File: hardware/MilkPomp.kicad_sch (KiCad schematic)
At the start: 0 parts

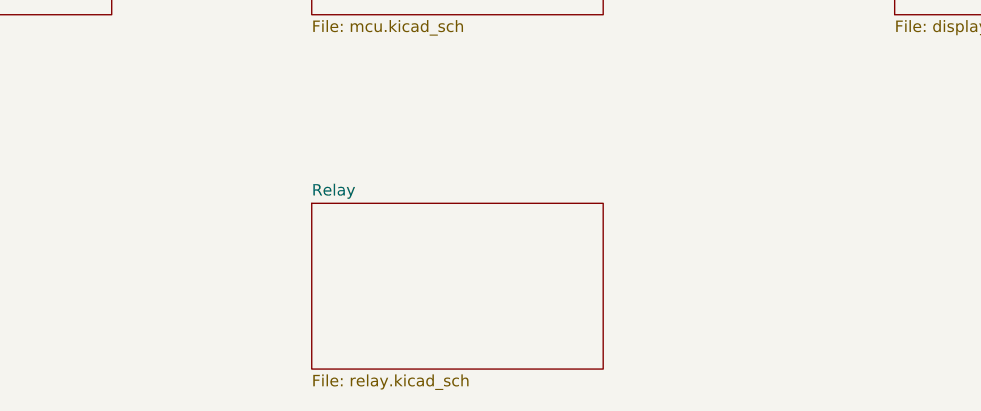
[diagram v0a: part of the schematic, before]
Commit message: Relay module completed
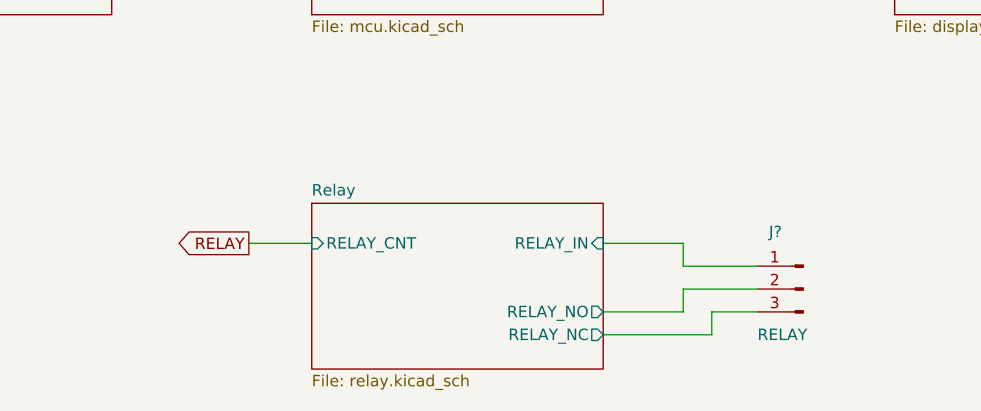
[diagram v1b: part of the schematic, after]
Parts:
- added J?: RELAY, symbol Connector:Conn_01x03_Male
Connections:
- new net Relay/RELAY_IN: J?.1 (Pin_1)
- new net Relay/RELAY_NC: J?.3 (Pin_3)
- new net Relay/RELAY_NO: J?.2 (Pin_2)
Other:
- sheet Relay ports: added RELAY_CNT, RELAY_IN, RELAY_NC, RELAY_NO; removed none

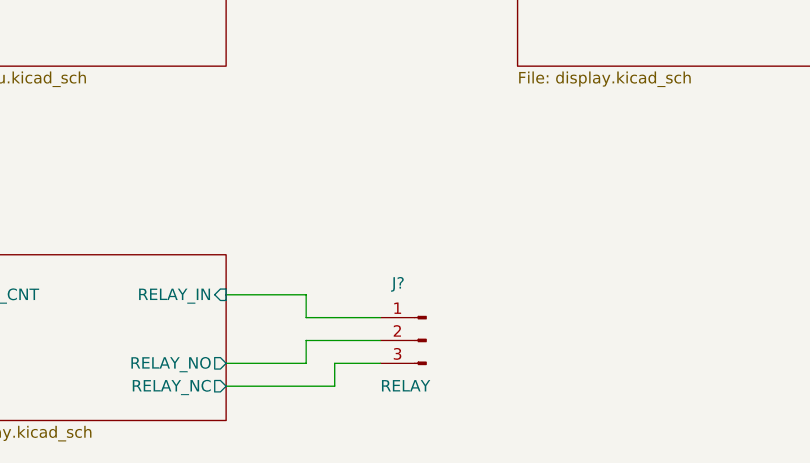
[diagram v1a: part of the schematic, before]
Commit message: Display circuit added
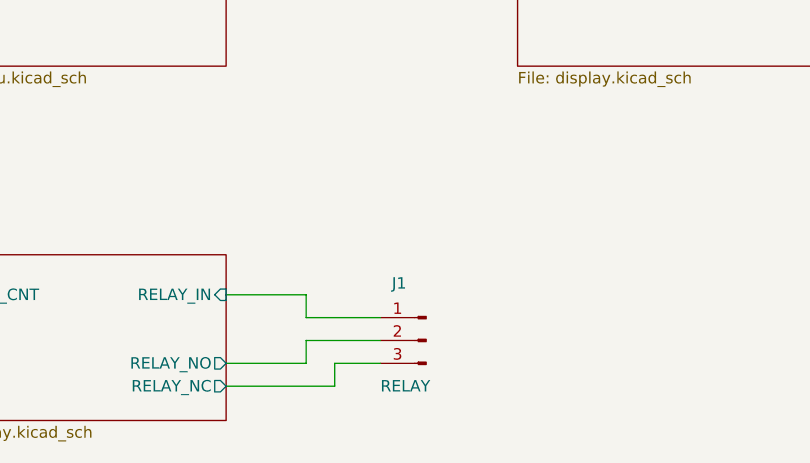
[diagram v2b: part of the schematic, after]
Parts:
- gave numbers to parts that had none: 1

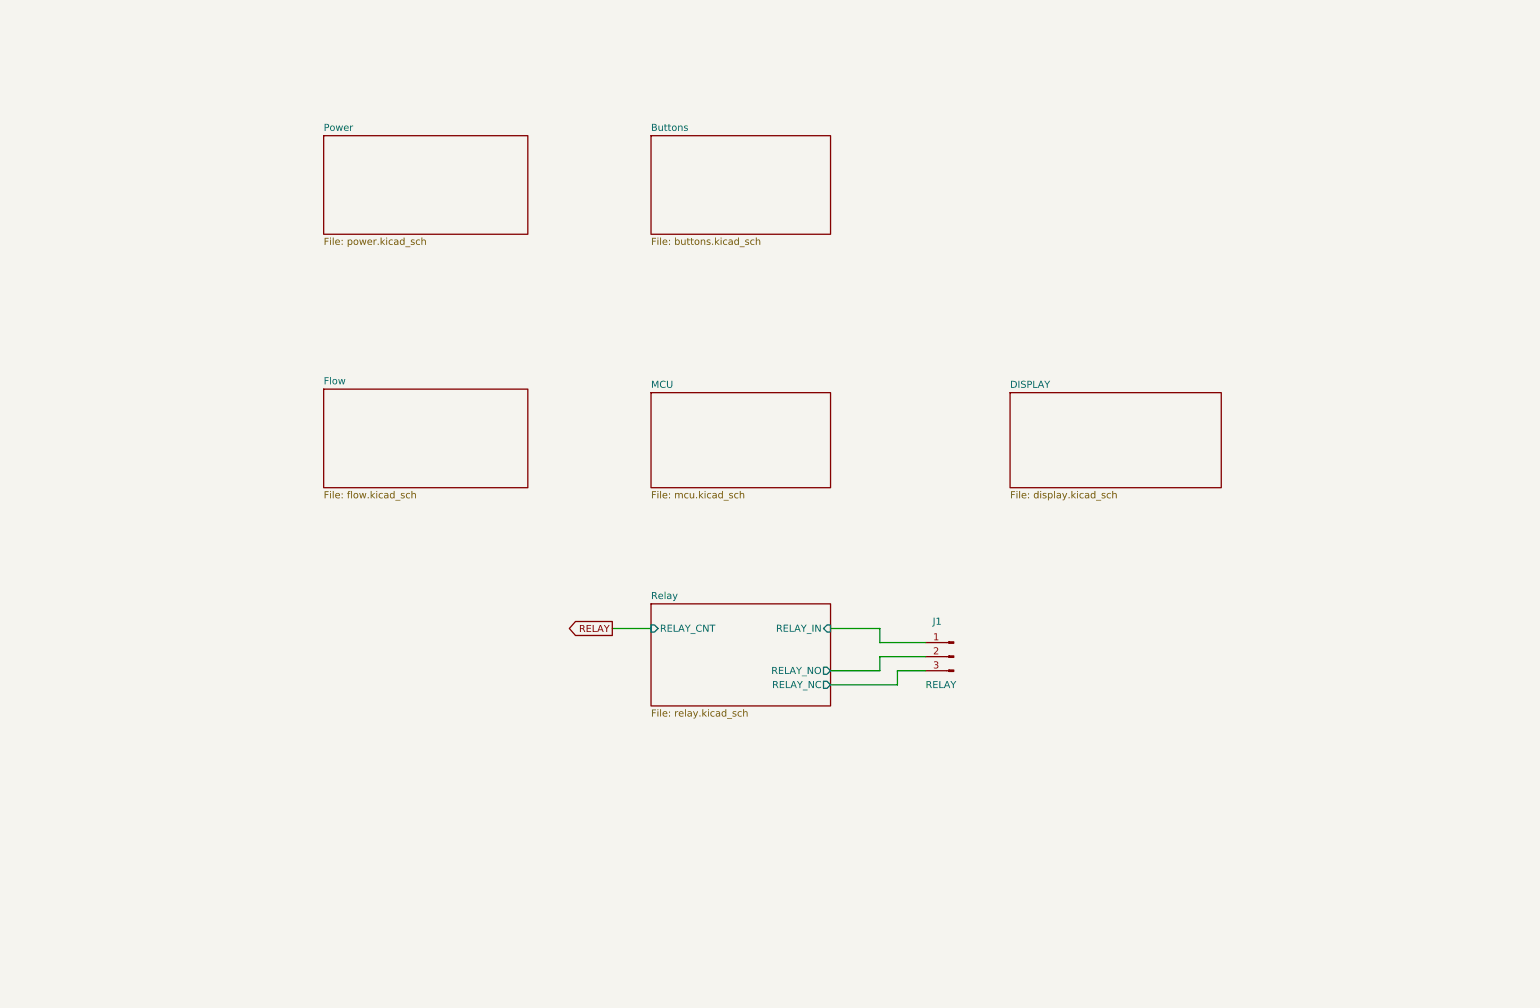
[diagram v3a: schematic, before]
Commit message: Schematics are completed
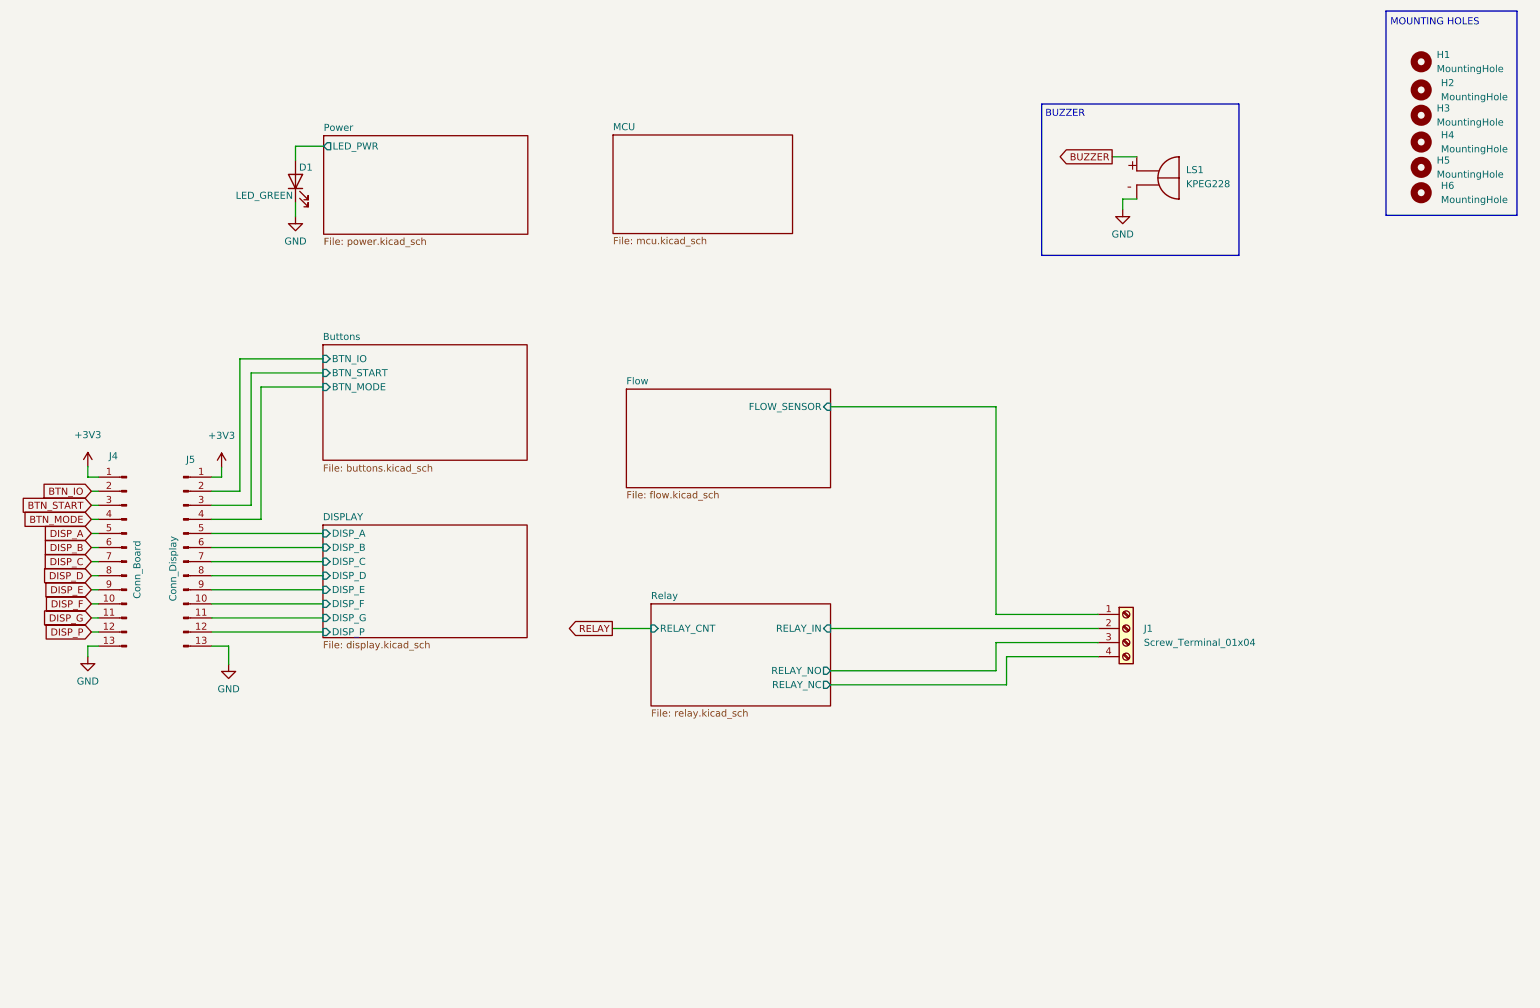
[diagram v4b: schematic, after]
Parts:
- removed J1: RELAY, symbol Connector:Conn_01x03_Male
- added D1: LED_GREEN, LED_SMD:LED_1206_3216Metric, symbol Device:LED
- added H1, H2, H3, H4, H5, H6: MountingHole, MountingHole:MountingHole_2.5mm, symbol Mechanical:MountingHole
- added J1: Screw_Terminal_01x04, Connector_Phoenix_MC:PhoenixContact_MC_1,5_4-G-3.81_1x04_P3.81mm_Horizontal, symbol Connector:Screw_Terminal_01x04
- added J4: Conn_Board, Connector_JST:JST_EH_B13B-EH-A_1x13_P2.50mm_Vertical, symbol Connector:Conn_01x13_Male
- added J5: Conn_Display, Connector_JST:JST_EH_B13B-EH-A_1x13_P2.50mm_Vertical, symbol Connector:Conn_01x13_Male
- added LS1: KPEG228, Buzzer:XDCR_KPEG228, symbol KPEG228:KPEG228
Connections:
- net Relay/RELAY_IN: now also J1.2 (Pin_2)
- net Relay/RELAY_NC: now also J1.4 (Pin_4)
- net Relay/RELAY_NO: now also J1.3 (Pin_3)
- new net +3V3: J4.1 (Pin_1), J5.1 (Pin_1)
- new net BTN_IO: J4.2 (Pin_2)
- new net BTN_MODE: J4.4 (Pin_4)
- new net BTN_START: J4.3 (Pin_3)
- new net BUZZER: LS1.P
- new net Buttons/BTN_IO: J5.2 (Pin_2)
- new net Buttons/BTN_MODE: J5.4 (Pin_4)
- new net Buttons/BTN_START: J5.3 (Pin_3)
- new net DISPLAY/DISP_A: J5.5 (Pin_5)
- new net DISPLAY/DISP_B: J5.6 (Pin_6)
- new net DISPLAY/DISP_C: J5.7 (Pin_7)
- new net DISPLAY/DISP_D: J5.8 (Pin_8)
- new net DISPLAY/DISP_E: J5.9 (Pin_9)
- new net DISPLAY/DISP_F: J5.10 (Pin_10)
- new net DISPLAY/DISP_G: J5.11 (Pin_11)
- new net DISPLAY/DISP_P: J5.12 (Pin_12)
- new net DISP_A: J4.5 (Pin_5)
- new net DISP_B: J4.6 (Pin_6)
- new net DISP_C: J4.7 (Pin_7)
- new net DISP_D: J4.8 (Pin_8)
- new net DISP_E: J4.9 (Pin_9)
- new net DISP_F: J4.10 (Pin_10)
- new net DISP_G: J4.11 (Pin_11)
- new net DISP_P: J4.12 (Pin_12)
- new net Flow/FLOW_SENSOR: J1.1 (Pin_1)
- new net GND: D1.1 (K), J4.13 (Pin_13), J5.13 (Pin_13), LS1.N
- new net Power/LED_PWR: D1.2 (A)
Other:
- sheet Buttons ports: added BTN_IO, BTN_MODE, BTN_START; removed none
- sheet DISPLAY ports: added DISP_A, DISP_B, DISP_C, DISP_D, DISP_E, DISP_F, DISP_G, DISP_P; removed none
- sheet Flow ports: added FLOW_SENSOR; removed none
- sheet Power ports: added LED_PWR; removed none
- note added: "BUZZER"
- note added: "MOUNTING HOLES"

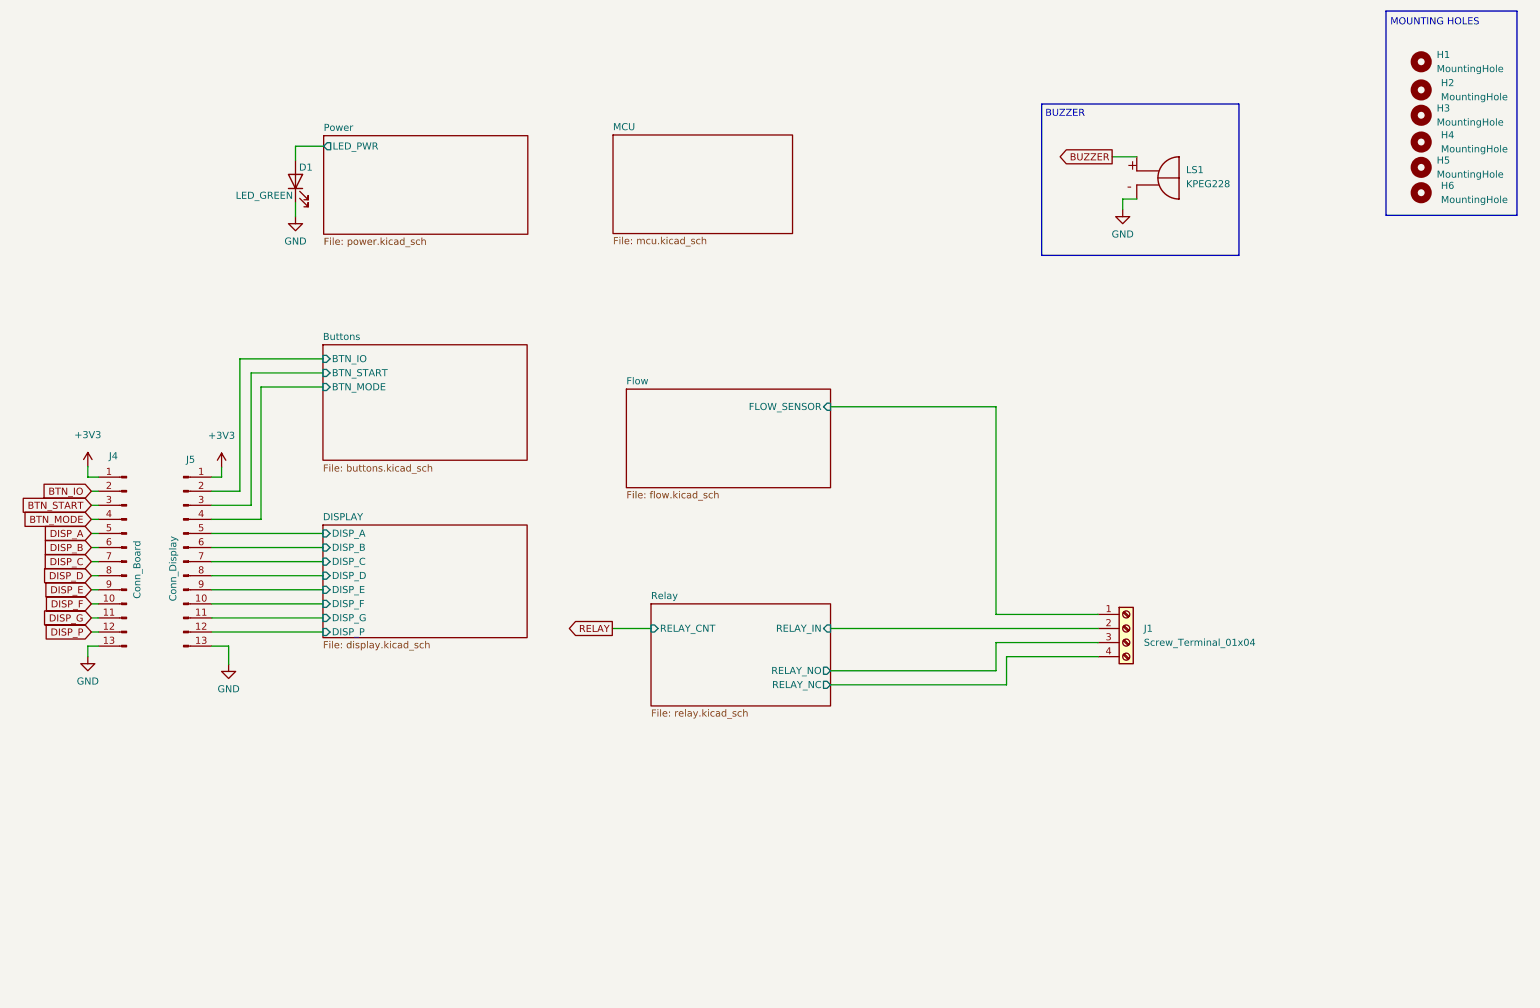
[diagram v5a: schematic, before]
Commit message: Footprints are assigned and Cut edges fixed
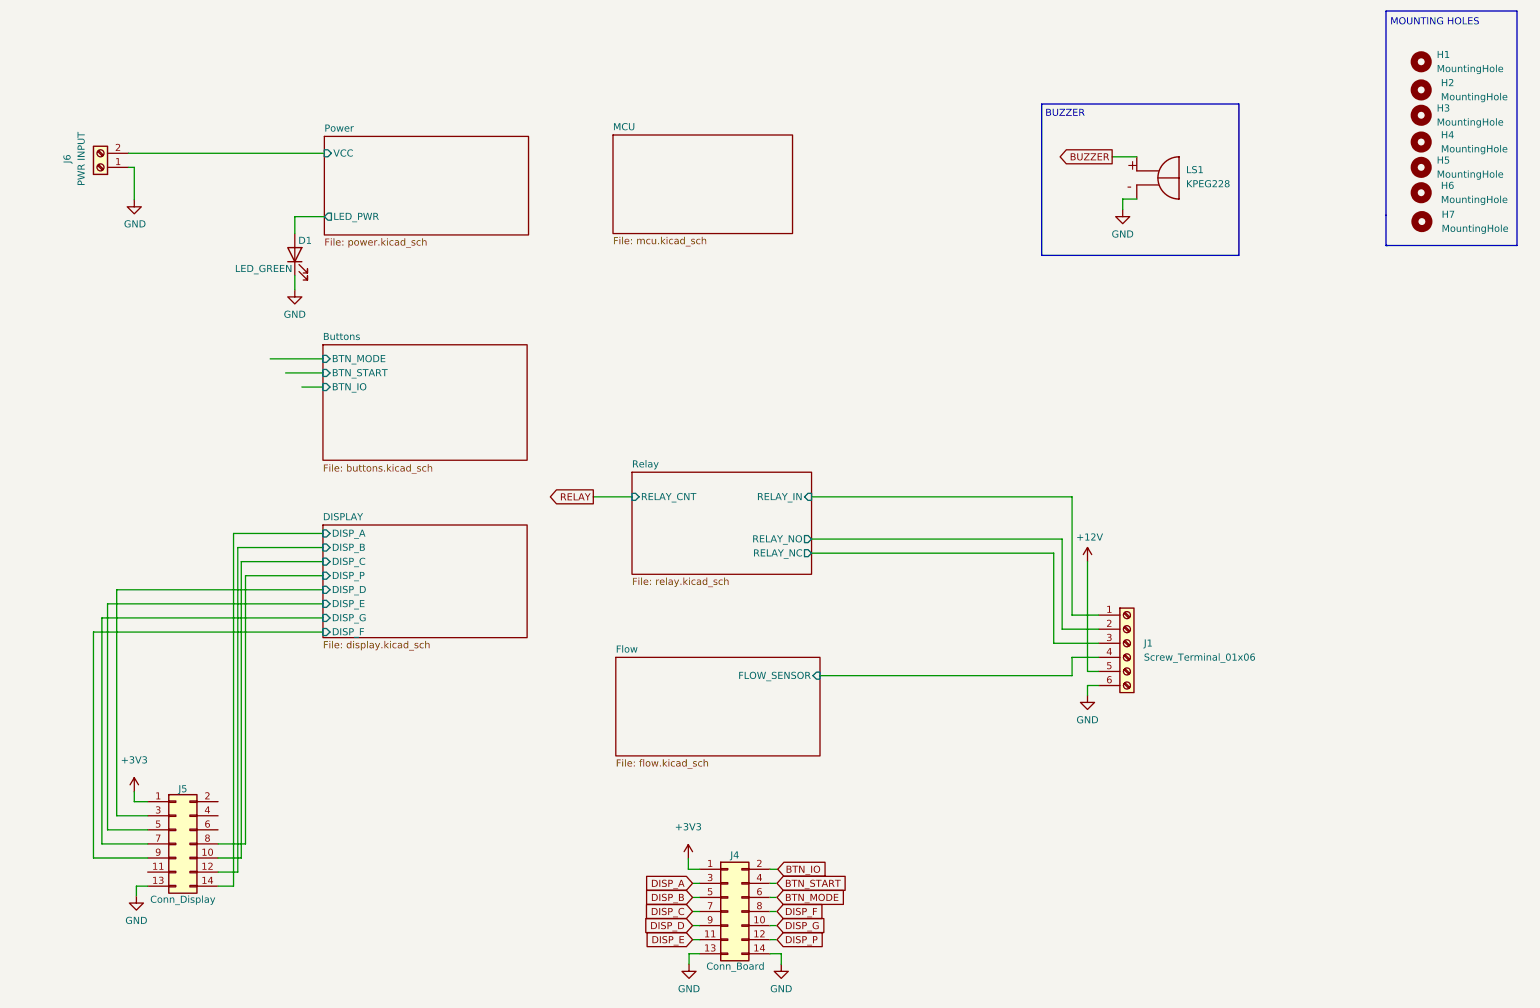
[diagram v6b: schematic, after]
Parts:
- removed J1: Screw_Terminal_01x04, Connector_Phoenix_MC:PhoenixContact_MC_1,5_4-G-3.81_1x04_P3.81mm_Horizontal, symbol Connector:Screw_Terminal_01x04
- removed J4: Conn_Board, Connector_JST:JST_EH_B13B-EH-A_1x13_P2.50mm_Vertical, symbol Connector:Conn_01x13_Male
- removed J5: Conn_Display, Connector_JST:JST_EH_B13B-EH-A_1x13_P2.50mm_Vertical, symbol Connector:Conn_01x13_Male
- added H7: MountingHole, MountingHole:MountingHole_2.5mm, symbol Mechanical:MountingHole
- added J1: Screw_Terminal_01x06, Connector_Phoenix_MSTB:PhoenixContact_MSTBA_2,5_6-G-5,08_1x06_P5.08mm_Horizontal, symbol Connector:Screw_Terminal_01x06
- added J4: Conn_Board, Connector_Multicomp:Multicomp_MC9A12-1434_2x07x2.54mm_Straight, symbol Connector_Generic:Conn_02x07_Odd_Even
- added J5: Conn_Display, Connector_Multicomp:Multicomp_MC9A12-1434_2x07x2.54mm_Straight, symbol Connector_Generic:Conn_02x07_Odd_Even
- added J6: PWR INPUT, Connector_Phoenix_MSTB:PhoenixContact_MSTBA_2,5_2-G_1x02_P5.00mm_Horizontal, symbol Connector:Screw_Terminal_01x02
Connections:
- net +3V3: now also J4.1 (Pin_1), J5.1 (Pin_1)
- net BTN_IO: now also J4.2 (Pin_2)
- net BTN_MODE: now also J4.6 (Pin_6)
- net BTN_START: now also J4.4 (Pin_4)
- net DISPLAY/DISP_A: now also J5.14 (Pin_14)
- net DISPLAY/DISP_B: now also J5.12 (Pin_12)
- net DISPLAY/DISP_C: now also J5.10 (Pin_10)
- net DISPLAY/DISP_D: now also J5.3 (Pin_3)
- net DISPLAY/DISP_E: now also J5.5 (Pin_5)
- net DISPLAY/DISP_F: now also J5.9 (Pin_9)
- net DISPLAY/DISP_G: now also J5.7 (Pin_7)
- net DISPLAY/DISP_P: now also J5.8 (Pin_8)
- net DISP_A: now also J4.3 (Pin_3)
- net DISP_B: now also J4.5 (Pin_5)
- net DISP_C: now also J4.7 (Pin_7)
- net DISP_D: now also J4.9 (Pin_9)
- net DISP_E: now also J4.11 (Pin_11)
- net DISP_F: now also J4.8 (Pin_8)
- net DISP_G: now also J4.10 (Pin_10)
- net DISP_P: now also J4.12 (Pin_12)
- net Flow/FLOW_SENSOR: now also J1.4 (Pin_4)
- net GND: now also J1.6 (Pin_6), J4.13 (Pin_13), J4.14 (Pin_14), J5.13 (Pin_13), J6.1 (Pin_1)
- net Relay/RELAY_IN: now also J1.1 (Pin_1)
- net Relay/RELAY_NC: now also J1.3 (Pin_3)
- net Relay/RELAY_NO: now also J1.2 (Pin_2)
- new net +12V: J1.5 (Pin_5)
- new net Power/VCC: J6.2 (Pin_2)
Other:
- sheet Power ports: added VCC; removed none
- moved on the sheet: D1

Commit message: PCB drawing completed
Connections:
- net +3V3: now also J4.13 (Pin_13), J5.13 (Pin_13); no longer J4.1 (Pin_1), J5.1 (Pin_1)
- net BTN_IO: now also J4.6 (Pin_6); no longer J4.2 (Pin_2)
- net BTN_MODE: now also J4.2 (Pin_2); no longer J4.6 (Pin_6)
- net Buttons/BTN_IO: now also J5.6 (Pin_6)
- net Buttons/BTN_MODE: now also J5.2 (Pin_2)
- net Buttons/BTN_START: now also J5.4 (Pin_4)
- net DISPLAY/DISP_A: now also J5.8 (Pin_8); no longer J5.14 (Pin_14)
- net DISPLAY/DISP_B: now also J5.10 (Pin_10); no longer J5.12 (Pin_12)
- net DISPLAY/DISP_C: now also J5.12 (Pin_12); no longer J5.10 (Pin_10)
- net DISPLAY/DISP_D: now also J5.11 (Pin_11); no longer J5.3 (Pin_3)
- net DISPLAY/DISP_E: now also J5.9 (Pin_9); no longer J5.5 (Pin_5)
- net DISPLAY/DISP_F: now also J5.5 (Pin_5); no longer J5.9 (Pin_9)
- net DISPLAY/DISP_P: now also J5.14 (Pin_14); no longer J5.8 (Pin_8)
- net DISP_A: now also J4.8 (Pin_8); no longer J4.3 (Pin_3)
- net DISP_B: now also J4.10 (Pin_10); no longer J4.5 (Pin_5)
- net DISP_C: now also J4.12 (Pin_12); no longer J4.7 (Pin_7)
- net DISP_D: now also J4.11 (Pin_11); no longer J4.9 (Pin_9)
- net DISP_E: now also J4.9 (Pin_9); no longer J4.11 (Pin_11)
- net DISP_F: now also J4.5 (Pin_5); no longer J4.8 (Pin_8)
- net DISP_G: now also J4.7 (Pin_7); no longer J4.10 (Pin_10)
- net DISP_P: now also J4.14 (Pin_14); no longer J4.12 (Pin_12)
- net GND: now also J4.1 (Pin_1), J4.3 (Pin_3), J5.1 (Pin_1), J5.3 (Pin_3); no longer J4.13 (Pin_13), J4.14 (Pin_14), J5.13 (Pin_13)
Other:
- moved on the sheet: J5
